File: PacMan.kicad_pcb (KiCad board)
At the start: 2 copper layers, 134.6 x 109.2 mm, 160 parts, among them J1 POWER+, J10 SEG+ CellMen, J13 AIR Left, J14 AIR Right, J2 POWER-, J4 Charge Detection, J5 SEG- CellMen, J6 BusBar Current Sensor, J7 Panel, J8 SLOOP, J9 GLV/CAN, K1 G5Q-1A4 DC24, K2 T9AS1D12-24, K3 T9AS1D12-24, Q1 DMN3730U, Q2 DMN3730U, Q4 DMP10H4D2S, Q5 DMP10H4D2S, U1 MCP9804, U10 LTC4151, U11 INA592, U12 MEF1S2405SP3C, U13 V7805-500, U14 Si8600AC, U15 Si8600AC, U16 TEC3-2419, U17 TEC3-2419, U18 AP2204K-5.0, U21 Si8600AC, U22 AP2204K-5.0, U3 ADM6320, U4 MCP2551-I-SN, U5 ESP32_DEVKITC, U6 MCP23008, U7 BQ32002, U8 ACHS-7122, U9 PDQE10-Q48-S24-D, Y1 32K

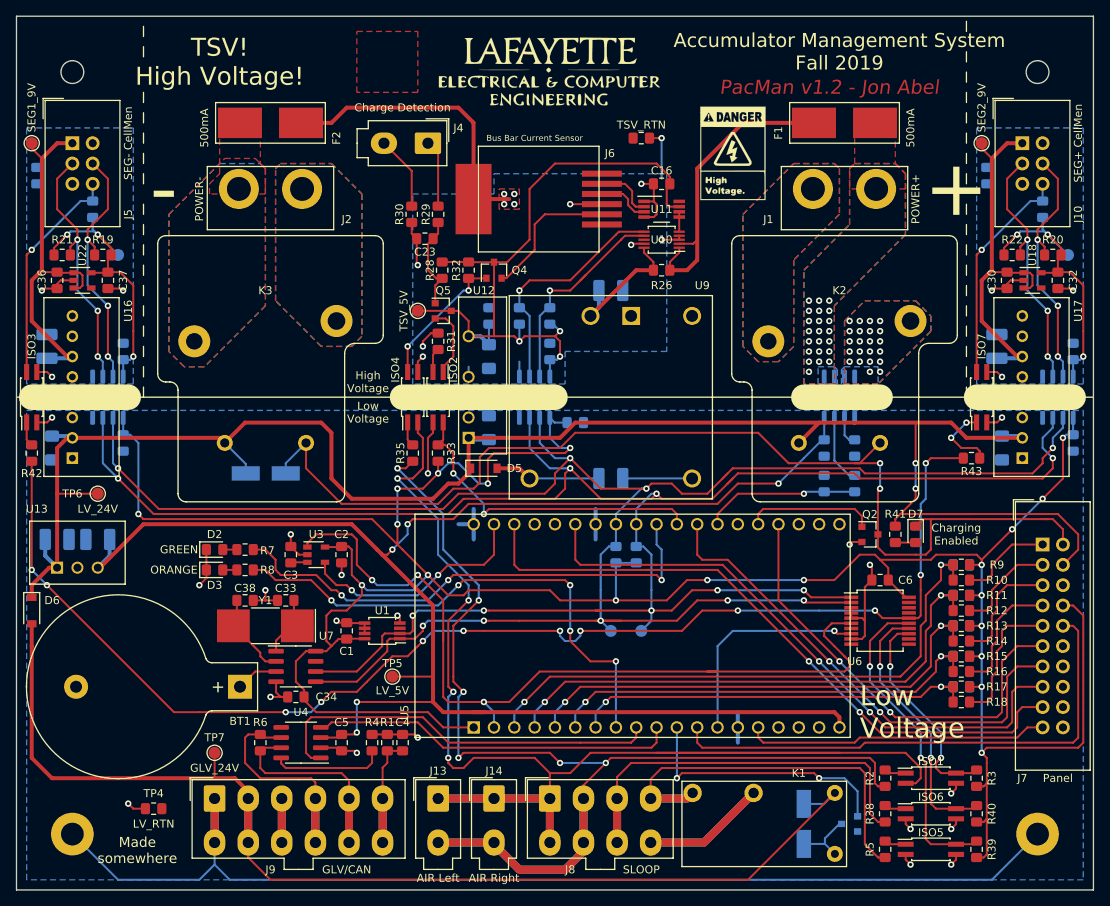
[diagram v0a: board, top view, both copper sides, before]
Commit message: Updated PCB design to match schematic changes, played with spacings
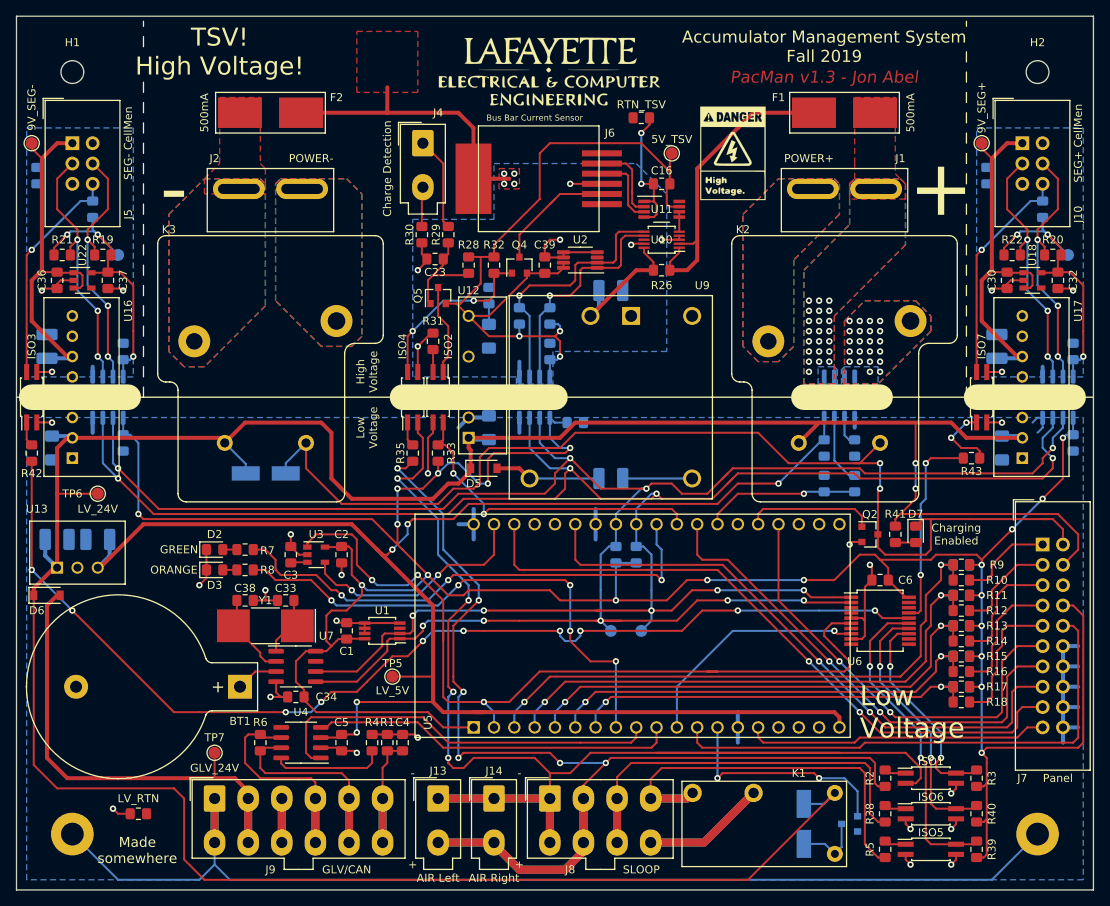
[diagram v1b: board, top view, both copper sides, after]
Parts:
- removed G***: LOGO, Lafayette_Electric_Car_Footprints:pacman_github_link
- added C39: 0.1u/50V, Capacitor_SMD:C_0805_2012Metric_Pad1.15x1.40mm_HandSolder, F.Cu at (142.2, 75.6)
- added U2: MCP9804, Package_SO:MSOP-8_3x3mm_P0.65mm, F.Cu at (146.7, 74.9)
- H1, H2: value MountingHole_Pad_#4 -> MountingHole_NoPad_#4
- J1, J2: footprint Lafayette_Electric_Car_Footprints:Powerpole_PP45_FP_1x2_NoSlot -> Lafayette_Electric_Car_Footprints:Powerpole_PP45_FP_1x2
- R19, R20, R21, R22, R23, R27, R44, R45: value 4.7k -> 3.3k
- R2, R35, R38, R5: value 4.7k -> 5.1k
- R31: value R -> 330
- R41: value R -> 1k
- R42, R43: value R -> 270
- TP1: value SEG1_5V -> 5V_SEG-
- TP10: value TSV_5V -> 5V_TSV
- TP11: value TSV_RTN -> RTN_TSV
- TP12: value SEG2_9V -> 9V_SEG+
- TP13: value SEG2_5V -> 5V_SEG+
- TP14: value SEG2_RTN -> RTN_SEG+
- TP2: value SEG1_RTN -> RTN_SEG-
- TP3: value SEG1_9V -> 9V_SEG-
- U12: footprint Lafayette_Electric_Car_Footprints:VIFSD1-S24-S5-SIP -> Lafayette_Electric_Car_Footprints:MEF1S2405SP3C
- moved TP10 37.4 mm to (158.1, 61.6), turned to 180 degrees
- moved R28 3.36 mm to (132.7, 75.6)
- moved Q4 3.24 mm to (139.1, 75.6)
- moved R32 3.24 mm to (135.9, 75.6)
- moved R29 2.84 mm to (130.2, 71.8)
- moved R30 2.84 mm to (126.9, 71.8)
- moved C23 2.84 mm to (128.5, 74.8)
- moved D6 2.69 mm to (80.0, 116.8), turned to 0 degrees
- moved C27 2.54 mm to (135.3, 84.5)
- moved J6 2.54 mm to (141.5, 64.8)
- moved R34 2.54 mm to (135.3, 79.4)
- moved TP11 2.54 mm to (154.3, 57.1)
- moved TP4 2.01 mm to (91.4, 144.1)
- moved Q5 2.01 mm to (128.9, 79.4), turned to 90 degrees
- moved F1 1.27 mm to (179.7, 56.5)
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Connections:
- net /RST_SEG1 renamed /RST_SEG-
- net /RST_SEG2 renamed /RST_SEG+
- net /SCL_SEG1 renamed /SCL_SEG-
- net /SCL_SEG2 renamed /SCL_SEG+
- net /SDA_SEG1 renamed /SDA_SEG-
- net /SDA_SEG2 renamed /SDA_SEG+
- net /SEG1_5V renamed /5V_SEG-
- net /SEG1_9V renamed /9V_SEG-
- net /SEG1_RTN renamed /RTN_SEG-
- net /SEG2_5V renamed /5V_SEG+
- net /SEG2_9V renamed /9V_SEG+
- net /SEG2_RTN renamed /RTN_SEG+
- C16 pad 2: /TSV_5V -> /5V_TSV
- C27 pad 1: /TSV_5V -> /5V_TSV
- C35 pad 1: /TSV_5V -> /5V_TSV
- D1 pad 1: /GLV_24V -> /LV_24V
- J10 pad 5: Net-(J10-Pad5) -> (no net)
- J5 pad 5: Net-(J5-Pad5) -> (no net)
- J6 pad 1: Net-(J6-Pad1) -> (no net)
- J6 pad 6: Net-(J6-Pad6) -> (no net)
- J7 pad 6: Net-(J7-Pad6) -> (no net)
- K1 pad 1: /GLV_24V -> /LV_24V
- Q4 pad 2: /AMPS_PWR -> /5V_TSV
- Q4 pad 3: /TSV_5V -> /AMPS_PWR
- Q5 pad 2: Net-(ISO2-Pad1) -> /5V_TSV
- Q5 pad 3: /TSV_5V -> Net-(ISO2-Pad1)
- R28 pad 1: /TSV_5V -> /5V_TSV
- R32 pad 1: /TSV_5V -> /5V_TSV
- R34 pad 1: /TSV_5V -> /5V_TSV
- R42 pad 2: /RST_GLV -> /RST_GLV_SEG-
- R43 pad 2: /RST_GLV -> /RST_GLV_SEG+
- R44 pad 1: /TSV_5V -> /5V_TSV
- R45 pad 1: /TSV_5V -> /5V_TSV
- TP10 pad 1: /TSV_5V -> /5V_TSV
- U1 pad 3: Net-(U1-Pad3) -> (no net)
- U10 pad 8: Net-(U10-Pad8) -> (no net)
- U11 pad 7: /TSV_5V -> /5V_TSV
- U11 pad 8: Net-(U11-Pad8) -> (no net)
- U16 pad 3: Net-(U16-Pad3) -> (no net)
- U17 pad 3: Net-(U17-Pad3) -> (no net)
- U18 pad 4: Net-(U18-Pad4) -> (no net)
- U21 pad 8: /TSV_5V -> /5V_TSV
- U22 pad 4: Net-(U22-Pad4) -> (no net)
- U4 pad 5: Net-(U4-Pad5) -> (no net)
- U5 pad 11: /MCU/SLOOP_EN -> /MCU/IO_INT
- U5 pad 13: /MCU/IO_INT -> /MCU/SLOOP_EN
- U5 pad 16: Net-(U5-Pad16) -> (no net)
- U5 pad 17: Net-(U5-Pad17) -> (no net)
- U5 pad 18: Net-(U5-Pad18) -> (no net)
- U5 pad 23: Net-(U5-Pad23) -> (no net)
- U5 pad 24: Net-(U5-Pad24) -> (no net)
- U5 pad 33: Net-(U5-Pad33) -> (no net)
- U5 pad 36: Net-(U5-Pad36) -> (no net)
- U5 pad 37: Net-(U5-Pad37) -> (no net)
- U5 pad 38: Net-(U5-Pad38) -> (no net)
- U6 pad 10: Net-(U6-Pad10) -> (no net)
- U6 pad 11: Net-(U6-Pad11) -> (no net)
- U6 pad 12: Net-(U6-Pad12) -> (no net)
- U6 pad 16: /RST_GLV -> /RST_GLV_SEG-
- U6 pad 17: Net-(U6-Pad17) -> /RST_GLV_SEG+
- U6 pad 18: Net-(U6-Pad18) -> (no net)
- U6 pad 19: Net-(U6-Pad19) -> (no net)
- U6 pad 7: Net-(U6-Pad7) -> (no net)
- U7 pad 7: Net-(U7-Pad7) -> (no net)
- U9 pad 6: Net-(U9-Pad6) -> (no net)
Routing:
- net /RST_GLV: track 163.9 -> 0.00 mm, vias 12 -> 0
- net /LV_24V: track 233.6 -> 373.6 mm
- net /RST_GLV_SEG-: track 0.00 -> 138.0 mm, vias 0 -> 10
- net /5V_TSV: track 0.00 -> 99.5 mm, vias 0 -> 3
- net /TSV_5V: track 89.2 -> 0.00 mm, vias 3 -> 0
- net /GLV_24V: track 145.9 -> 63.2 mm
- net /GLV_RTN: track 106.4 -> 143.9 mm, vias 20 -> 19
- net /RST_GLV_SEG+: track 0.00 -> 25.2 mm, vias 0 -> 2
- net /PACK_RTN: track 74.4 -> 84.6 mm
- net /MCU/SLOOP_EN: track 33.3 -> 28.2 mm
- net /Isolation/EN_AMPS: track 17.5 -> 22.4 mm
- net /CHRG_DETECT-: track 9.30 -> 4.96 mm
- net /CHRG_DETECT+: track 8.39 -> 11.7 mm
- net /DCHRG_A2: track 7.34 -> 10.2 mm
- net /DCHRG_A1: track 6.64 -> 9.40 mm
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- removed copper zone on F.Cu, net (none)
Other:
- board text added: "PacMan v1.3 - Jon Abel"
- board text removed: "500mA"
- board text removed: "PacMan v1.2 - Jon Abel"

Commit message: added GLV measurement point, switched to a 16 pin 4 in 1 isolator
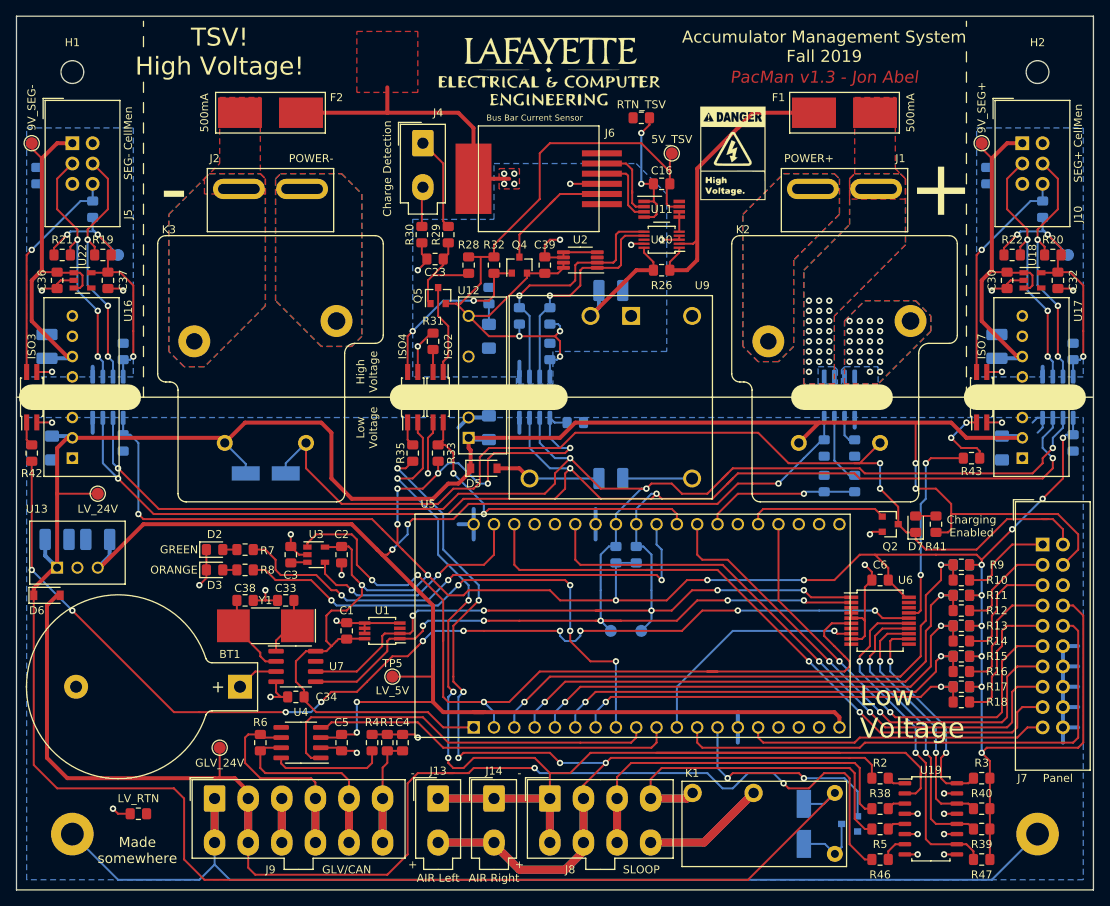
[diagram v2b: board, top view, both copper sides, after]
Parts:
- removed ISO1, ISO5, ISO6: TLP293, Package_SO:SO-4_4.4x2.3mm_P1.27mm
- added R46: 5.1k, Resistor_SMD:R_0805_2012Metric_Pad1.15x1.40mm_HandSolder, F.Cu at (184.2, 149.9)
- added R47: 10k, Resistor_SMD:R_0805_2012Metric_Pad1.15x1.40mm_HandSolder, F.Cu at (196.8, 149.9)
- added U19: TLP293-4, Package_SO:SOIC-16_4.55x10.3mm_P1.27mm, F.Cu at (190.5, 144.8)
- moved R41 5.24 mm to (191.1, 108.0), turned to 90 degrees
- moved Q2 2.84 mm to (185.4, 108.0)
- moved R39 2.62 mm to (196.8, 146.1), turned to 0 degrees
- moved R5 2.62 mm to (184.2, 146.1), turned to 180 degrees
- moved D7 1.27 mm to (188.6, 108.0), turned to 90 degrees
- moved R38 0.90 mm to (184.2, 143.5), turned to 180 degrees
- moved R40 0.90 mm to (196.8, 143.5), turned to 0 degrees
- moved TP7 0.90 mm to (101.6, 135.9)
- moved R2 0.63 mm to (184.2, 139.7), turned to 180 degrees
- moved R3 0.63 mm to (196.8, 139.7), turned to 0 degrees
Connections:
- U6 pad 12: (no net) -> /MCU/AIRS_STATUS
- U6 pad 13: /MCU/AIRS_STATUS -> /MCU/SLOOP2_STATUS
- U6 pad 14: /MCU/SLOOP2_STATUS -> /MCU/SLOOP1_STATUS
- U6 pad 15: /MCU/SLOOP1_STATUS -> /MCU/GLV_STATUS
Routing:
- net /GLV_24V: track 63.2 -> 169.4 mm, vias 0 -> 2
- net /MCU/GLV_STATUS: track 0.00 -> 42.9 mm, vias 0 -> 2
- net /LV_24V: track 373.6 -> 363.7 mm
- net /CHRG_LED: track 136.5 -> 128.6 mm
- net /SLOOP1_IN: track 53.2 -> 48.2 mm
- net /GLV_RTN: track 143.9 -> 147.8 mm, vias 19 -> 21
- net /MCU/SLOOP1_STATUS: track 40.2 -> 36.8 mm
- net Net-(R46-Pad1): track 0.00 -> 3.46 mm
- net /LV_3V3: track 355.0 -> 351.9 mm
- net /SLOOP2: track 77.2 -> 74.1 mm
- net /AIRS+: track 162.3 -> 159.7 mm
- net /AIRS-: track 181.4 -> 183.4 mm
- net /MCU/SLOOP2_STATUS: track 33.3 -> 31.8 mm
- net /CHRG_EN: track 16.2 -> 17.5 mm
- net /MCU/SLOOP_EN: track 28.2 -> 27.4 mm

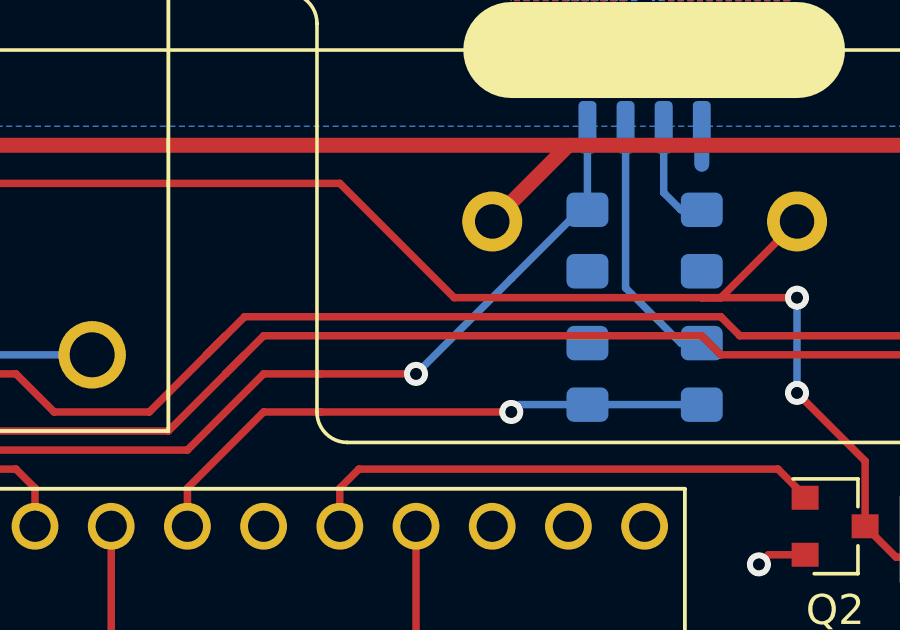
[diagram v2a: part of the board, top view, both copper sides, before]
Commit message: added filter cap to ADC measurement channel
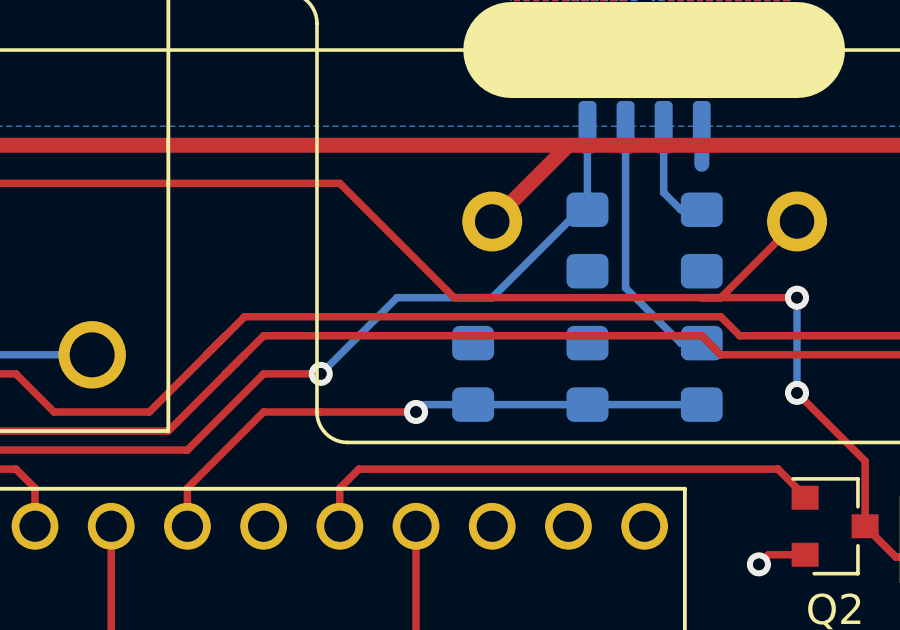
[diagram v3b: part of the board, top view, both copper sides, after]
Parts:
- added C40: C, Capacitor_SMD:C_0805_2012Metric_Pad1.15x1.40mm_HandSolder, B.Cu at (173.4, 102.9)

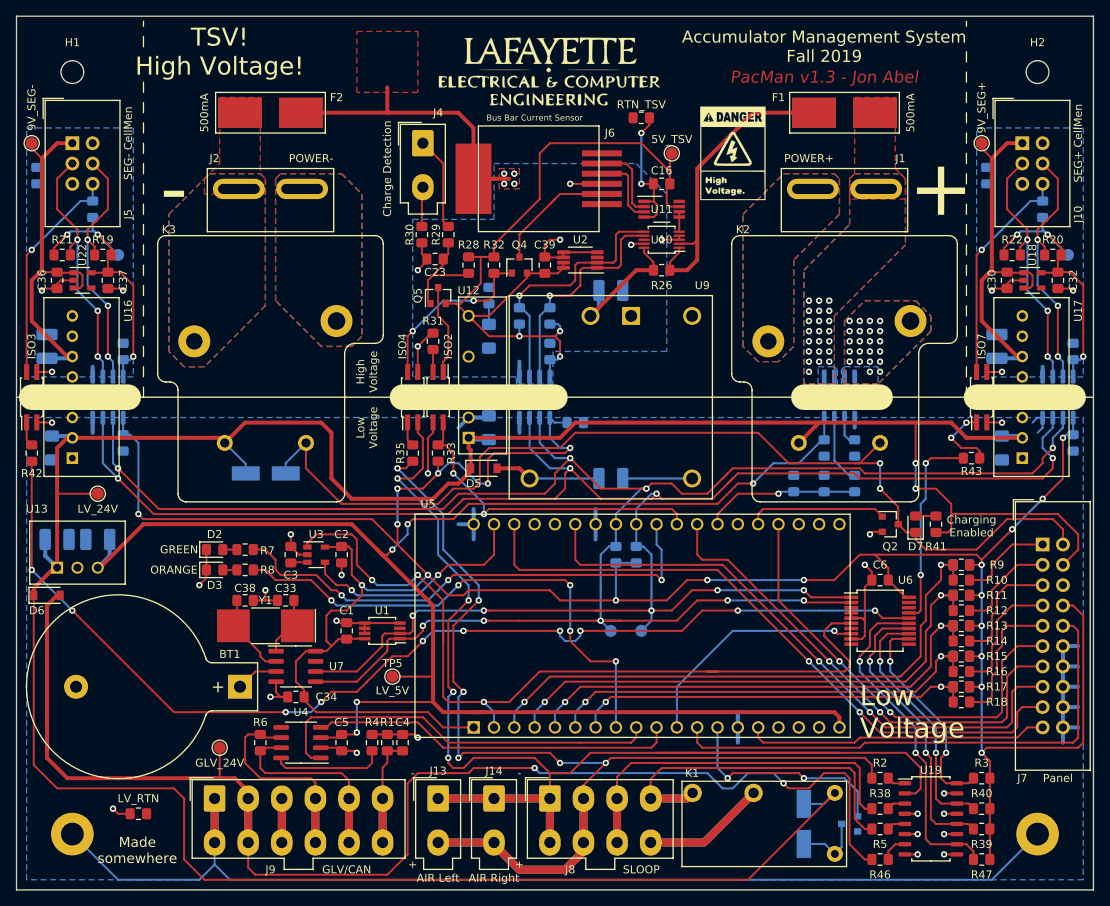
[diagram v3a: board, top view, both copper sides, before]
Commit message: Fixed the issue with the ADC pins (VP and VN), did some rerouting, slight silkscreen changes
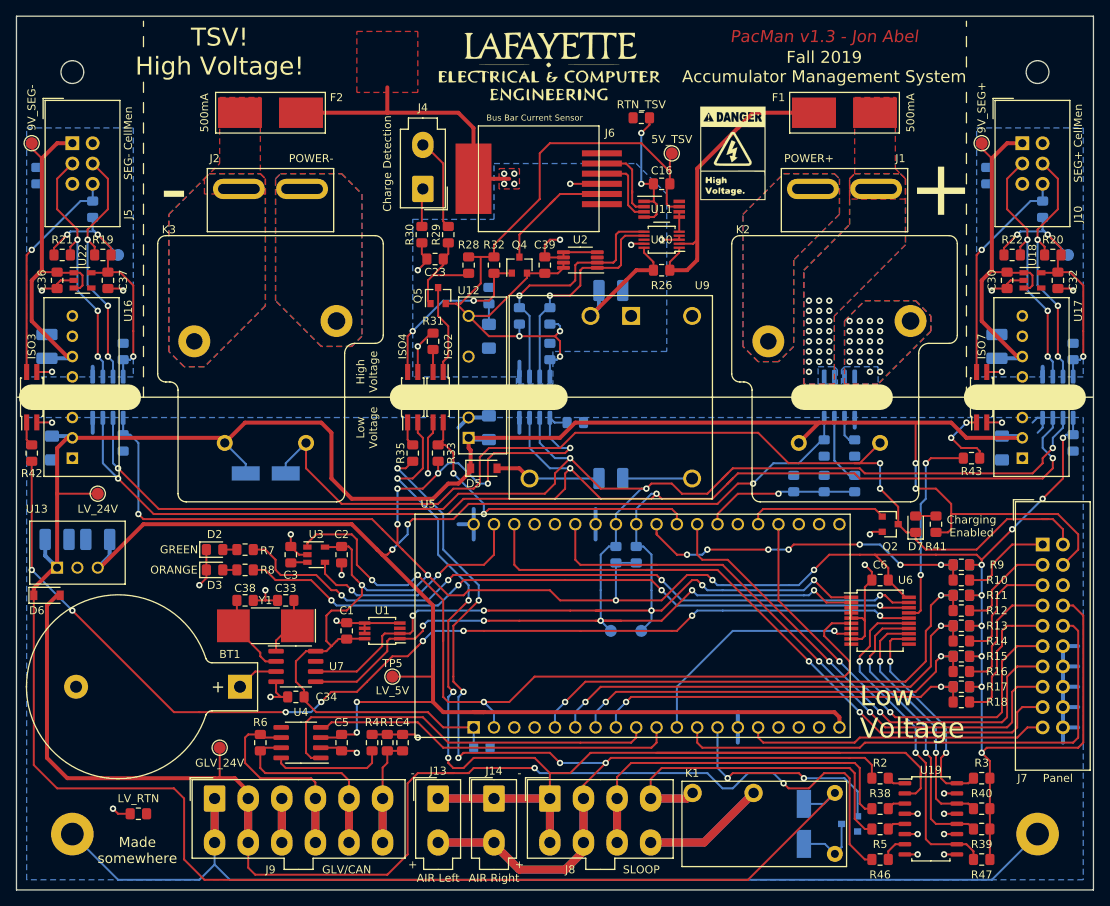
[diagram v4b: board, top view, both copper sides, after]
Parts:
- added C41: 0.1u/50V, Capacitor_SMD:C_0805_2012Metric_Pad1.15x1.40mm_HandSolder, B.Cu at (134.4, 135.9)
- moved J4 5.72 mm to (127.0, 66.0), turned to 180 degrees
- moved LOGO1 0.64 mm to (142.9, 50.8)
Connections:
- J4 pad 1: /CHRG_DETECT+ -> /CHRG_DETECT-
- J4 pad 2: /CHRG_DETECT- -> /CHRG_DETECT+
- U5 pad 29: /MCU/LED1 -> /MCU/BTN_LEFT_MCU
- U5 pad 3: /MCU/BTN_LEFT_MCU -> (no net)
- U5 pad 4: /MCU/BTN_RIGHT_MCU -> (no net)
- U5 pad 5: /MCU/BTN_UP_MCU -> /MCU/BTN_RIGHT_MCU
- U5 pad 6: /MCU/BTN_DOWN_MCU -> /MCU/BTN_UP_MCU
- U5 pad 7: /MCU/BTN_CENTER_MCU -> /MCU/BTN_DOWN_MCU
- U5 pad 8: /MCU/LED2 -> /MCU/BTN_CENTER_MCU
- U6 pad 18: (no net) -> /MCU/LED2
- U6 pad 19: (no net) -> /MCU/LED1
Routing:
- net /MCU/BTN_LEFT_MCU: track 73.0 -> 44.4 mm, vias 2 -> 7
- net /MCU/LED1: track 63.2 -> 88.6 mm, vias 3 -> 4
- net /MCU/LED2: track 65.0 -> 86.5 mm, vias 5 -> 4
- net /LV_3V3: track 351.9 -> 355.5 mm
- net /MCU/BTN_UP_MCU: track 61.8 -> 59.3 mm
- net /MCU/BTN_DOWN_MCU: track 56.2 -> 53.7 mm
- net /MCU/BTN_CENTER_MCU: track 51.3 -> 48.8 mm
- net /MCU/BTN_RIGHT_MCU: track 67.4 -> 64.9 mm
- net /SCL_GLV: track 247.3 -> 249.4 mm
- net /RST_GLV_SEG-: track 138.0 -> 136.2 mm, vias 10 -> 8
- net /SDA_GLV: track 244.6 -> 246.2 mm
- net /MCU/~RESET: track 105.0 -> 104.1 mm
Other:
- board text added: "Fall 2019 Accumulator Management System"
- board text removed: "Accumulator Management System Fall 2019"
